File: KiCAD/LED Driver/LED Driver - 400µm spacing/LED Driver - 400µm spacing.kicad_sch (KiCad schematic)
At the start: 9 parts, among them U1 LP5868TRKPR, U2 ATtiny3226

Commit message: low-volt cutoff, indicator LED, and mounting bolts added
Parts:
- removed HS1: Heatsink, Custom:heatsink, symbol Mechanical:Heatsink
- added D2: LED, LED_SMD:LED_0201_0603Metric, symbol Device:LED
- added H1, H2, H3, H4: MountingHole, Custom:M1 hole, symbol Mechanical:MountingHole
- added Q1: Q_NMOS_GSD, Custom:SOT-323_SC-70 - thin, symbol Device:Q_NMOS_GSD
- added TP2: UPDI Pogo Pads, Custom:1mm pad, symbol Connector:Conn_01x03_Pin
- added U3: XC61GC3002HR-G, Custom:XC61G_USP-3_TOR, symbol Custom:XC61GC3002HR-G
- C4: footprint Capacitor_SMD:C_0402_1005Metric_Pad0.74x0.62mm_HandSolder -> Capacitor_SMD:C_0402_1005Metric
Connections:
- net Col1: now also D2.2 (A)
- net GND: now also U2.11 (6/PB3), Q1.3 (D), TP2.1 (Pin_1)
- net Photodiode: no longer U2.8 (3/PA7)
- net UPDI: now also TP2.2 (Pin_2)
- net at U1.9 (CS8): now also D2.1 (K)
- net +5V renamed +BATT
- net +BATT: now also TP2.3 (Pin_3), U3.3 (VIN)
- new net: Q1.1 (G), U3.2 (VOUT)
- new net -BATT: Q1.2 (S), U3.1 (VSS)
- no-connect marks 22 -> 21

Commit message: Working draft of programmer/charger board
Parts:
- added BT1: LiPo Cell, Custom:LPM0940, symbol Device:Battery_Cell
- TP2: footprint Custom:1mm pad -> Custom:1mm pad x4; symbol Connector:Conn_01x03_Pin -> Connector:Conn_01x04_Pin
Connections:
- net +BATT: now also BT1.1 (+)
- net -BATT: now also TP2.4 (Pin_4), BT1.2 (-)
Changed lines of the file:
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@@
+	)
+	(junction
+		(at 82.55 62.23)
+		(diameter 0)
+		(color 0 0 0 0)
 	)
 	(junction
@@
 	(wire
 		(pts
-			(xy 189.23 59.69) (xy 189.23 67.31)
+			(xy 82.55 69.85) (xy 92.71 69.85)
 		)
 		(stroke
@@
 	(wire
 		(pts
-			(xy 123.19 82.55) (xy 129.54 82.55)
+			(xy 189.23 59.69) (xy 189.23 67.31)
 		)
 		(stroke
@@
 	(wire
 		(pts
-			(xy 129.54 82.55) (xy 129.54 80.01)
+			(xy 82.55 62.23) (xy 85.09 62.23)
 		)
 		(stroke
@@
 	(wire
 		(pts
-			(xy 204.47 59.69) (xy 204.47 62.23)
+			(xy 123.19 82.55) (xy 129.54 82.55)
 		)
 		(stroke
@@
 	(wire
 		(pts
-			(xy 198.12 57.15) (xy 198.12 54.61)
+			(xy 129.54 82.55) (xy 129.54 80.01)
 		)
 		(stroke
@@
 	(wire
 		(pts
-			(xy 198.12 54.61) (xy 189.23 54.61)
+			(xy 204.47 59.69) (xy 204.47 62.23)
 		)
 		(stroke
@@
 	(wire
 		(pts
-			(xy 157.48 59.69) (xy 166.37 59.69)
+			(xy 198.12 57.15) (xy 198.12 54.61)
 		)
 		(stroke
@@
 	(wire
 		(pts
-			(xy 189.23 72.39) (xy 204.47 72.39)
+			(xy 198.12 54.61) (xy 189.23 54.61)
 		)
 		(stroke
@@
 	(wire
 		(pts
-			(xy 129.54 77.47) (xy 129.54 74.93)
+			(xy 157.48 59.69) (xy 166.37 59.69)
 		)
 		(stroke
@@
 	(wire
 		(pts
-			(xy 92.71 69.85) (xy 109.22 69.85)
+			(xy 189.23 72.39) (xy 204.47 72.39)
 		)
 		(stroke
@@
 	(wire
 		(pts
-			(xy 109.22 67.31) (xy 109.22 69.85)
+			(xy 129.54 77.47) (xy 129.54 74.93)
 		)
 		(stroke
@@
 	(wire
 		(pts
-			(xy 129.54 74.93) (xy 123.19 74.93)
+			(xy 92.71 69.85) (xy 109.22 69.85)
 		)
 		(stroke
@@
 	(wire
 		(pts
-			(xy 204.47 57.15) (xy 198.12 57.15)
+			(xy 109.22 67.31) (xy 109.22 69.85)
 		)
 		(stroke
@@
 	(wire
 		(pts
-			(xy 134.62 80.01) (xy 129.54 80.01)
+			(xy 129.54 74.93) (xy 123.19 74.93)
 		)
 		(stroke
@@
 	(wire
 		(pts
-			(xy 134.62 77.47) (xy 129.54 77.47)
+			(xy 204.47 57.15) (xy 198.12 57.15)
 		)
 		(stroke
@@
 	(wire
 		(pts
-			(xy 157.48 57.15) (xy 157.48 59.69)
+			(xy 134.62 80.01) (xy 129.54 80.01)
 		)
 		(stroke
@@
 	(wire
 		(pts
-			(xy 127 95.25) (xy 134.62 95.25)
+			(xy 134.62 77.47) (xy 129.54 77.47)
 		)
 		(stroke
@@
 	(wire
 		(pts
-			(xy 189.23 59.69) (xy 204.47 59.69)
+			(xy 157.48 57.15) (xy 157.48 59.69)
 		)
 		(stroke
@@
 	(wire
 		(pts
-			(xy 228.6 54.61) (xy 238.76 54.61)
+			(xy 127 95.25) (xy 134.62 95.25)
 		)
 		(stroke
@@
 		)
 	)
+	(wire
+		(pts
+			(xy 189.23 59.69) (xy 204.47 59.69)
+		)
+		(stroke
+			(width 0)
+			(type default)
+		)
+	)
+	(wire
+		(pts
+			(xy 228.6 54.61) (xy 238.76 54.61)
+		)
+		(stroke
+			(width 0)
+			(type default)
+		)
+	)
 	(label "Row1"
 		(at 157.48 102.87 0)
@@
 	)
 	(symbol
+		(lib_id "power:-BATT")
+		(at 238.76 49.53 90)
+		(unit 1)
+		(exclude_from_sim no)
+		(in_bom yes)
+		(on_board yes)
+		(dnp no)
+		(fields_autoplaced yes)
+		(property "Reference" "#PWR019"
+			(at 242.57 49.53 0)
+			(effects
+				(font
+					(size 1.27 1.27)
+				)
+				(hide yes)
+			)
+		)
+		(property "Value" "-BATT"
+			(at 235.585 49.53 90)
+			(effects
+				(font
+					(size 1.27 1.27)
+				)
+				(justify left)
+			)
+		)
+		(property "Footprint" ""
+			(at 238.76 49.53 0)
+			(effects
+				(font
+					(size 1.27 1.27)
+				)
+				(hide yes)
+			)
+		)
+		(property "Datasheet" ""
+			(at 238.76 49.53 0)
+			(effects
+				(font
+					(size 1.27 1.27)
+				)
+				(hide yes)
+			)
+		)
+		(property "Description" "Power symbol creates a global label with name \"-BATT\""
+			(at 238.76 49.53 0)
+			(effects
+				(font
+					(size 1.27 1.27)
+				)
+				(hide yes)
+			)
+		)
+		(pin "1"
+		)
+		(instances
+			(project "LED Driver - 400µm spacing"
+				(path "/333dbdf9-e35a-4a4e-87df-f2105d57feb4"
+					(reference "#PWR019")
+					(unit 1)
+				)
+			)
+		)
+	)
+	(symbol
 		(lib_id "Custom:ATtiny_3226")
 		(at 215.9 49.53 0)
@@
 	)
 	(symbol
-		(lib_id "power:+BATT")
-		(at 85.09 62.23 90)
+		(lib_id "Device:Battery_Cell")
+		(at 82.55 67.31 0)
 		(unit 1)
 		(exclude_from_sim no)
@@
 		(on_board yes)
 		(dnp no)
+		(property "Reference" "BT1"
+			(at 79.629 64.2563 0)
+			(effects
+				(font
+					(size 1.27 1.27)
+				)
+				(justify right)
+				(hide yes)
+			)
+		)
+		(property "Value" "LiPo Cell"
+			(at 79.629 66.6806 0)
+			(effects
+				(font
+					(size 1.27 1.27)
+				)
+				(justify right)
+			)
+		)
+		(property "Footprint" "Custom:LPM0940"
+			(at 82.55 65.786 90)
+			(effects
+				(font
+					(size 1.27 1.27)
+				)
+				(hide yes)
+			)
+		)
+		(property "Datasheet" "https://www.lipolbattery.com/Micro-Lithium-Battery-3.8V.html"
+			(at 82.55 65.786 90)
+			(effects
+				(font
+					(size 1.27 1.27)
+				)
+				(hide yes)
+			)
+		)
+		(property "Description" "25 mAh 0.89 g 9 mm x 4 mm"
+			(at 82.55 67.31 0)
+			(effects
+				(font
+					(size 1.27 1.27)
+				)
+				(hide yes)
+			)
+		)
+		(property "Manufacturer" "Lipol Battery"
+			(at 82.55 67.31 0)
+			(effects
+				(font
+					(size 1.27 1.27)
+				)
+				(hide yes)
+			)
+		)
+		(property "Part" "LPM0940"
+			(at 82.55 67.31 0)
+			(effects
+				(font
+					(size 1.27 1.27)
+				)
+				(hide yes)
+			)
+		)
+		(pin "2"
+		)
+		(pin "1"
+		)
+		(instances
+			(project ""
+				(path "/333dbdf9-e35a-4a4e-87df-f2105d57feb4"
+					(reference "BT1")
+					(unit 1)
+				)
+			)
+		)
+	)
+	(symbol
+		(lib_id "power:+BATT")
+		(at 82.55 62.23 90)
+		(unit 1)
+		(exclude_from_sim no)
+		(in_bom yes)
+		(on_board yes)
+		(dnp no)
 		(fields_autoplaced yes)
 		(property "Reference" "#PWR015"
-			(at 88.9 62.23 0)
+			(at 86.36 62.23 0)
 			(effects
 				(font
@@
 		)
 		(property "Value" "+BATT"
-			(at 81.915 62.23 90)
+			(at 79.375 62.23 90)
 			(effects
 				(font
@@
 		)
 		(property "Footprint" ""
-			(at 85.09 62.23 0)
+			(at 82.55 62.23 0)
 			(effects
 				(font
@@
 		)
 		(property "Datasheet" ""
-			(at 85.09 62.23 0)
+			(at 82.55 62.23 0)
 			(effects
 				(font
@@
 		)
 		(property "Description" "Power symbol creates a global label with name \"+BATT\""
-			(at 85.09 62.23 0)
+			(at 82.55 62.23 0)
 			(effects
 				(font
@@
 	)
 	(symbol
-		(lib_id "Connector:Conn_01x03_Pin")
+		(lib_id "Connector:Conn_01x04_Pin")
 		(at 243.84 54.61 180)
 		(unit 1)
@@
 		(fields_autoplaced yes)
 		(property "Reference" "TP2"
-			(at 244.5512 53.3978 0)
+			(at 244.5512 52.1278 0)
 			(effects
 				(font
@@
 		)
 		(property "Value" "UPDI Pogo Pads"
-			(at 244.5512 55.8221 0)
+			(at 244.5512 54.5521 0)
 			(effects
 				(font
@@
 			)
 		)
-		(property "Footprint" "Custom:1mm pad"
+		(property "Footprint" "Custom:1mm pad x4"
 			(at 243.84 54.61 0)
 			(effects
@@
 			)
 		)
-		(property "Description" "Generic connector, single row, 01x03, script generated"
+		(property "Description" "Generic connector, single row, 01x04, script generated"
 			(at 243.84 54.61 0)
 			(effects
@@
 		(pin "3"
 		)
-		(instances
+		(pin "4"
+		)
+		(instances

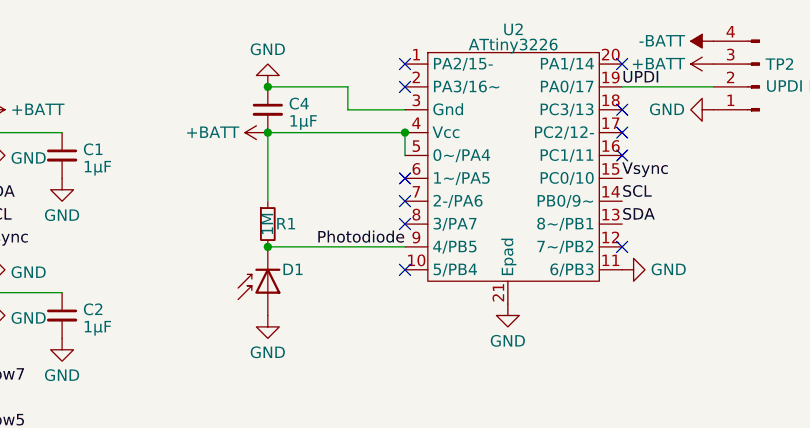
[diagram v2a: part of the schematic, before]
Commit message: Remove status pads for charger as DC-DC converter is required
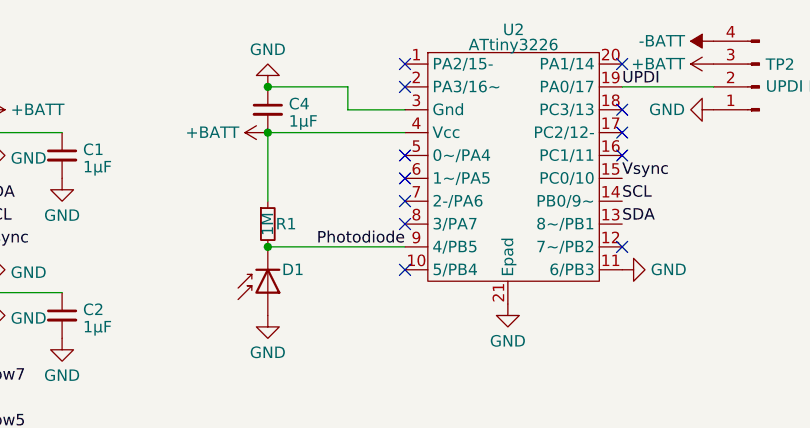
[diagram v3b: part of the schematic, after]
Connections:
- net +BATT: no longer U2.5 (0~/PA4)
- no-connect marks 21 -> 22
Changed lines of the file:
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@@
-	)
-	(junction
-		(at 204.47 59.69)
-		(diameter 0)
-		(color 0 0 0 0)
 	)
 	(junction
@@
 	(no_connect
 		(at 228.6 57.15)
+	)
+	(no_connect
+		(at 204.47 62.23)
 	)
 	(no_connect
@@
 		)
 		(stroke
-			(width 0)
-			(type default)
-		)
-	)
-	(wire
-		(pts
-			(xy 204.47 59.69) (xy 204.47 62.23)
-		)
-		(stroke
